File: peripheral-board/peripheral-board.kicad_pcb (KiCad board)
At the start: 2 copper layers, 165 x 130 mm, 264 parts, among them CON4001 BARREL_JACK, CON8001 SD_Card, J10001 DB15_FEMALE_HighDensity, J7001 FCR1295, P10001 VGA, P1001 Peripheral Bus, P1002 Power, Q4001 IRLML2244TRPbF, Q5001 IRLML2244TRPbF, Q5002 IRLML2244TRPbF, Q8001 BSS84LT1G, SW1001 Power, SW2001 1, SW2002 2, SW2003 3, SW2004 4, SW2005 5, SW2006 6, SW2007 7, SW2008 8, SW2009 9, SW2010 0, SW2011 +, SW2012 ´, SW2013 BKSP, SW2014 TROLL, SW2015 §, SW2016 UP, SW2017 RMB, SW2018 Q, SW2019 W, SW2020 E, SW2021 R, SW2022 T, SW2023 Y, SW2024 U, SW2025 I, SW2026 O, SW2027 P, SW2028 Å, SW2029 ¨, SW2030 RETURN, SW2031 ALT_GR, SW2032 <, SW2033 LEFT, SW2034 MMB, SW2035 A, SW2036 S, SW2037 D, SW2038 F, SW2039 G, SW2040 H, SW2041 J, SW2042 K, SW2043 L, SW2044 Ö, SW2045 Ä, SW2046 ', SW2047 ESC, SW2048 TAB, SW2049 ALT, SW2050 DOWN, SW2051 LMB, SW2052 SHIFT_L, SW2053 Z, SW2054 X, SW2055 C, SW2056 V, SW2057 B, SW2058 N, SW2059 M, SW2060 ,, SW2061 ., SW2062 -, SW2063 SHIFT_R, SW2064 FN_R, SW2065 SPACE, SW2066 FN_L, SW2067 RIGHT, SW2068 CTRL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

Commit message: minor fixes
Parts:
- added R2001: 0R, Resistors_SMD:R_1206, F.Cu at (93.9, 73.9)
- moved Q8001 4.01 mm to (91.5, 124.9), turned to 270 degrees
- moved C8002 3.40 mm to (126.2, 116.4)
- moved C8003 2.60 mm to (131.4, 114.2)
- moved D8001 2.55 mm to (173.5, 53.2), turned to 0 degrees
- moved C8004 2.50 mm to (126.2, 114.3)
- moved R4006 1.79 mm to (229.7, 55.6)
- moved R8003 1.50 mm to (178.9, 52.4)
- moved D4002 1.30 mm to (231.1, 53.1)
- moved R4008 1.19 mm to (232.3, 58.0)
- moved R4002 1.14 mm to (232.3, 56.0)
- moved C4001 0.85 mm to (234.8, 52.7)
- moved R4003 0.30 mm to (192.2, 51.3), turned to 180 degrees
- moved D1001 0.20 mm to (159.0, 53.2)
- moved D4003 0.20 mm to (164.9, 53.2)
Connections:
- U2003 pad 10: Net-(U2003-Pad10) -> Net-(R2001-Pad2)
- U2003 pad 6: Net-(U2003-Pad10) -> Net-(R2001-Pad1)
- U2003 pad 9: Net-(U2003-Pad10) -> Net-(R2001-Pad2)
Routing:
- net Net-(D8001-Pad2): track 0.00 -> 176.8 mm, vias 0 -> 2
- net +3V3: track 153.1 -> 246.3 mm, vias 2 -> 10
- net Net-(D4002-Pad1): track 2.51 -> 68.3 mm, vias 0 -> 1
- net GND: track 179.4 -> 232.9 mm, vias 7 -> 14
- net Net-(R4003-Pad1): track 0.00 -> 52.8 mm, vias 0 -> 1
- net Net-(R4004-Pad1): track 0.00 -> 41.2 mm, vias 0 -> 1
- net Net-(D4003-Pad1): track 0.00 -> 27.5 mm
- net Net-(D4003-Pad3): track 0.00 -> 22.5 mm
- net /KBD_Q0: track 430.1 -> 437.0 mm
- net Net-(R2001-Pad2): track 0.00 -> 6.07 mm
- net /KBD_Q1: track 538.7 -> 544.5 mm
- net Net-(D8001-Pad1): track 0.00 -> 5.37 mm
- net Net-(R2001-Pad1): track 0.00 -> 5.17 mm
- net /SPI_SS3: track 43.7 -> 47.7 mm
- net /Keyboard/COL5: track 74.9 -> 78.5 mm
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
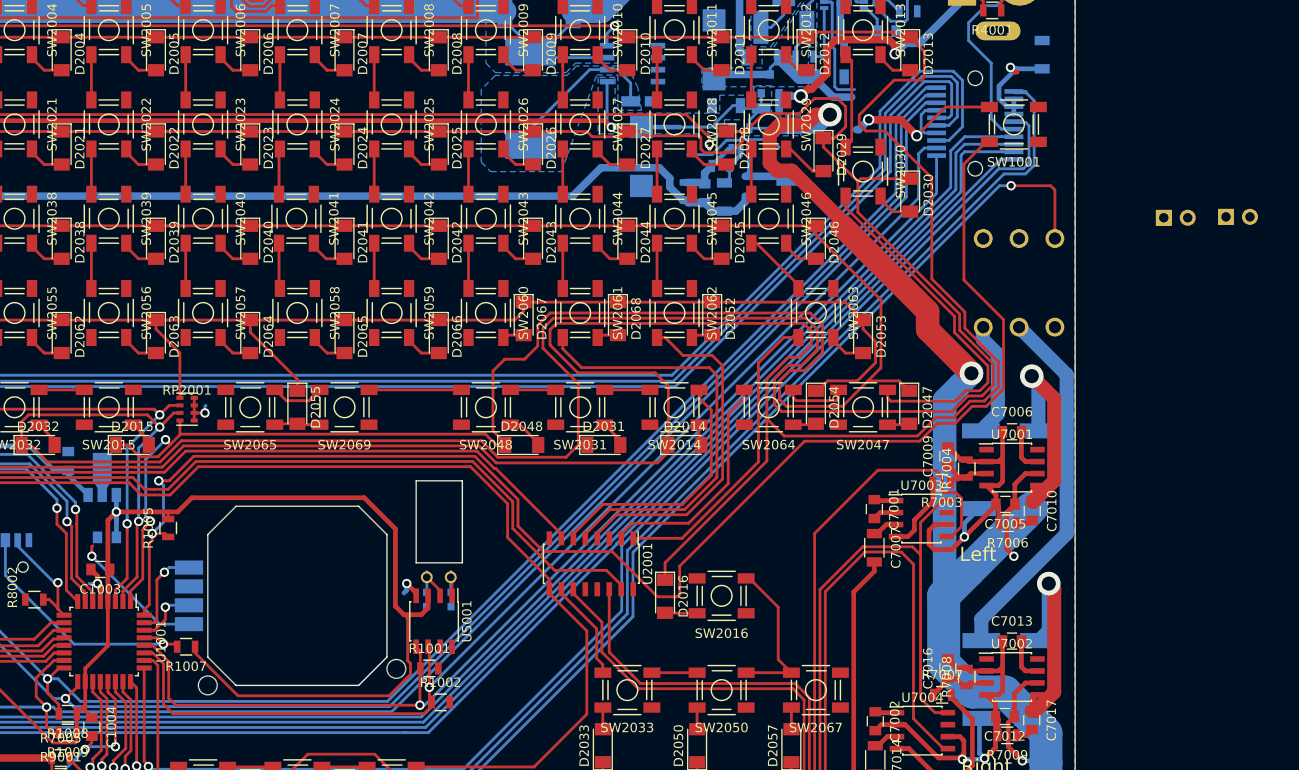
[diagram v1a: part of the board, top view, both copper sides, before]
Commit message: added speaker and battery connectors
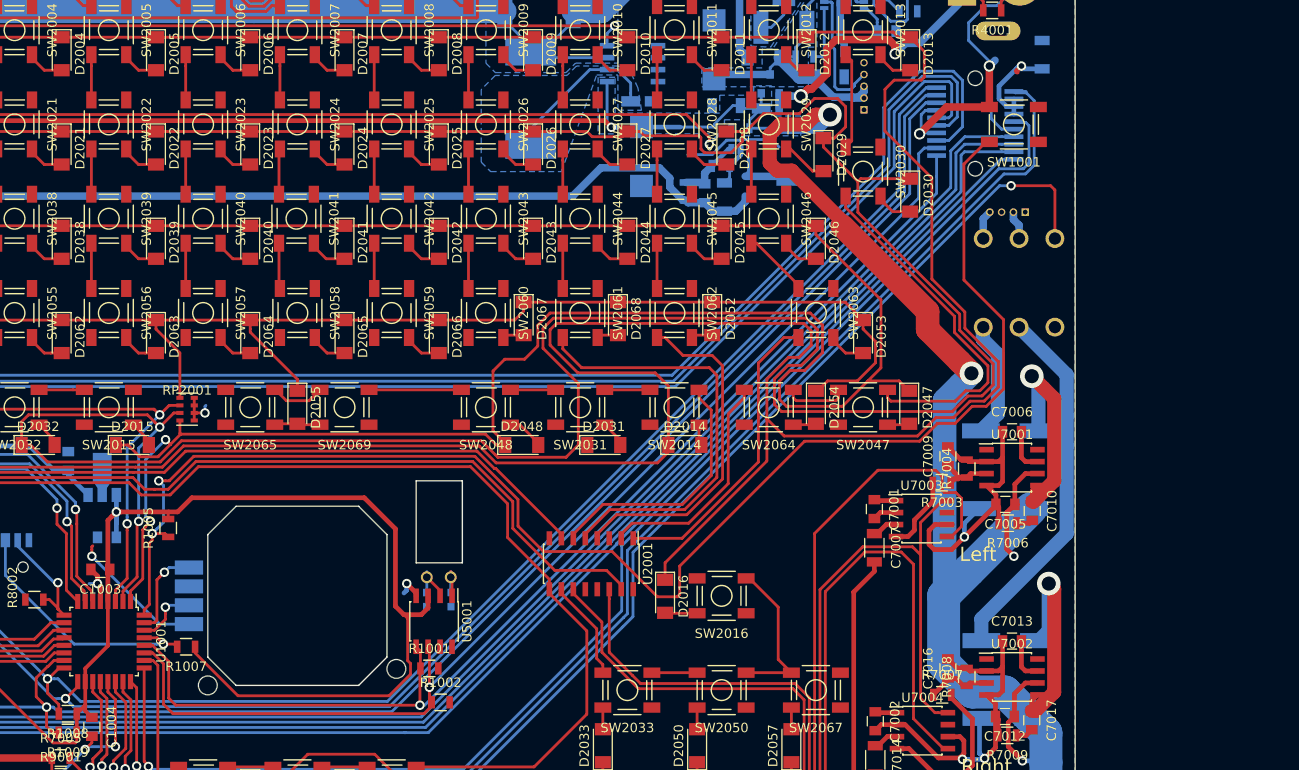
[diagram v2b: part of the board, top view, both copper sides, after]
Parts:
- removed LS7001: Speaker L, Socket_Strips:Socket_Strip_Straight_1x02_Pitch2.54mm
- removed LS7002: Speaker R, Socket_Strips:Socket_Strip_Straight_1x02_Pitch2.54mm
- added J4001: 53047-0510, Connectors_Molex:Connector_Molex_PicoBlade_53047-0510, B.Cu at (227.6, 68.5)
- added J7002: 53047-0310, Connectors_Molex:Connector_Molex_PicoBlade_53047-0410, B.Cu at (244.7, 79.3)
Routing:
- net +BATT: track 30.0 -> 33.5 mm
- net /KBD_Q0: track 437.0 -> 433.5 mm
- net /Audio/SPKR_L: track 0.00 -> 3.09 mm
- net /Audio/SPKR_R: track 0.00 -> 3.05 mm
- net GND: track 232.9 -> 229.9 mm
- net /Power Supply/BATTERY_NTC: track 12.1 -> 13.9 mm

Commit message: peripheral board all done o____O
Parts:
- removed J10001: DB15_FEMALE_HighDensity, lib:HDDSUB-15-VGA
- removed P10001: VGA, Socket_Strips:Socket_Strip_Straight_1x06
- removed Q5001, Q5002: IRLML2244TRPbF, TO_SOT_Packages_SMD:SOT-23
- removed R5001, R5006: 10k, Resistors_SMD:R_0805
- removed R5002, R5007: 150k, Resistors_SMD:R_0805
- removed R5003, R5004, R5008, R5009: 40R, Resistors_SMD:R_0805
- removed R5005, R5010: 220k, Resistors_SMD:R_0805
- removed RV5001, RV5002: 47k, lib:3364W
- removed TH5001: 10k, Capacitors_ThroughHole:CP_Radial_Tantal_D4.5mm_P2.50mm
- removed U5002, U5003: TL431, TO_SOT_Packages_SMD:SOT-23
- moved D2048 1.80 mm to (193.1, 104.0)
- moved R7003 1.10 mm to (234.8, 108.0)
- moved C7007 0.15 mm to (228.7, 115.0)
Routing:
- net GND: track 229.9 -> 291.5 mm, vias 14 -> 19
- net +3V3: track 246.3 -> 261.7 mm
- net /AUD_CS_L: track 145.9 -> 131.0 mm
- net /Keyboard/COL14: track 118.4 -> 123.6 mm
- net /KBD_Q0: track 433.5 -> 438.3 mm
- net /KBD_Q1: track 544.5 -> 548.9 mm
- net /AUD_UD: track 157.4 -> 161.0 mm
- net Net-(C7015-Pad1): track 23.4 -> 26.6 mm
- net Net-(D2048-Pad2): track 3.96 -> 5.64 mm
- net VAA: track 373.0 -> 371.5 mm
- net /KBD_Q2: track 443.8 -> 445.3 mm
- net /PWR_BTN: track 155.8 -> 157.3 mm
- net /Keyboard/COL2: track 177.3 -> 178.8 mm
- net /SD_DET: track 12.2 -> 11.3 mm
- net Net-(C7009-Pad1): track 5.97 -> 6.92 mm
- added copper zone on F.Cu, net GND
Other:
- board size 165 x 130 mm -> 165 x 100 mm

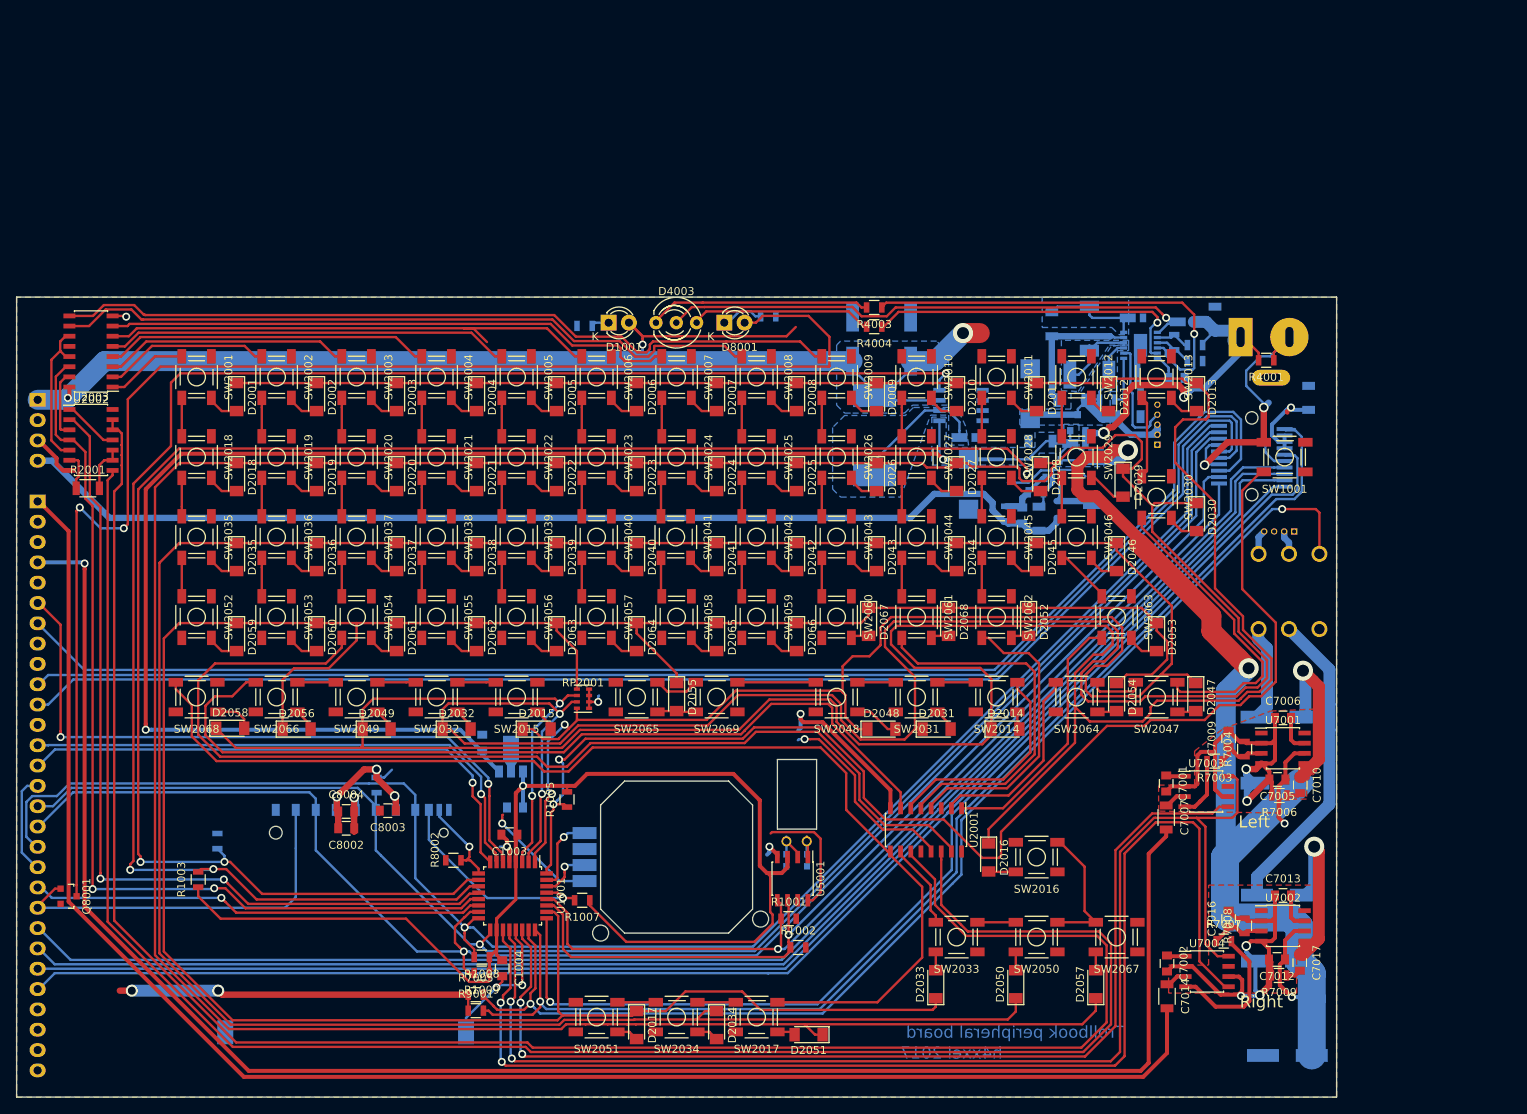
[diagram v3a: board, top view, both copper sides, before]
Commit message: touched up silkscreen
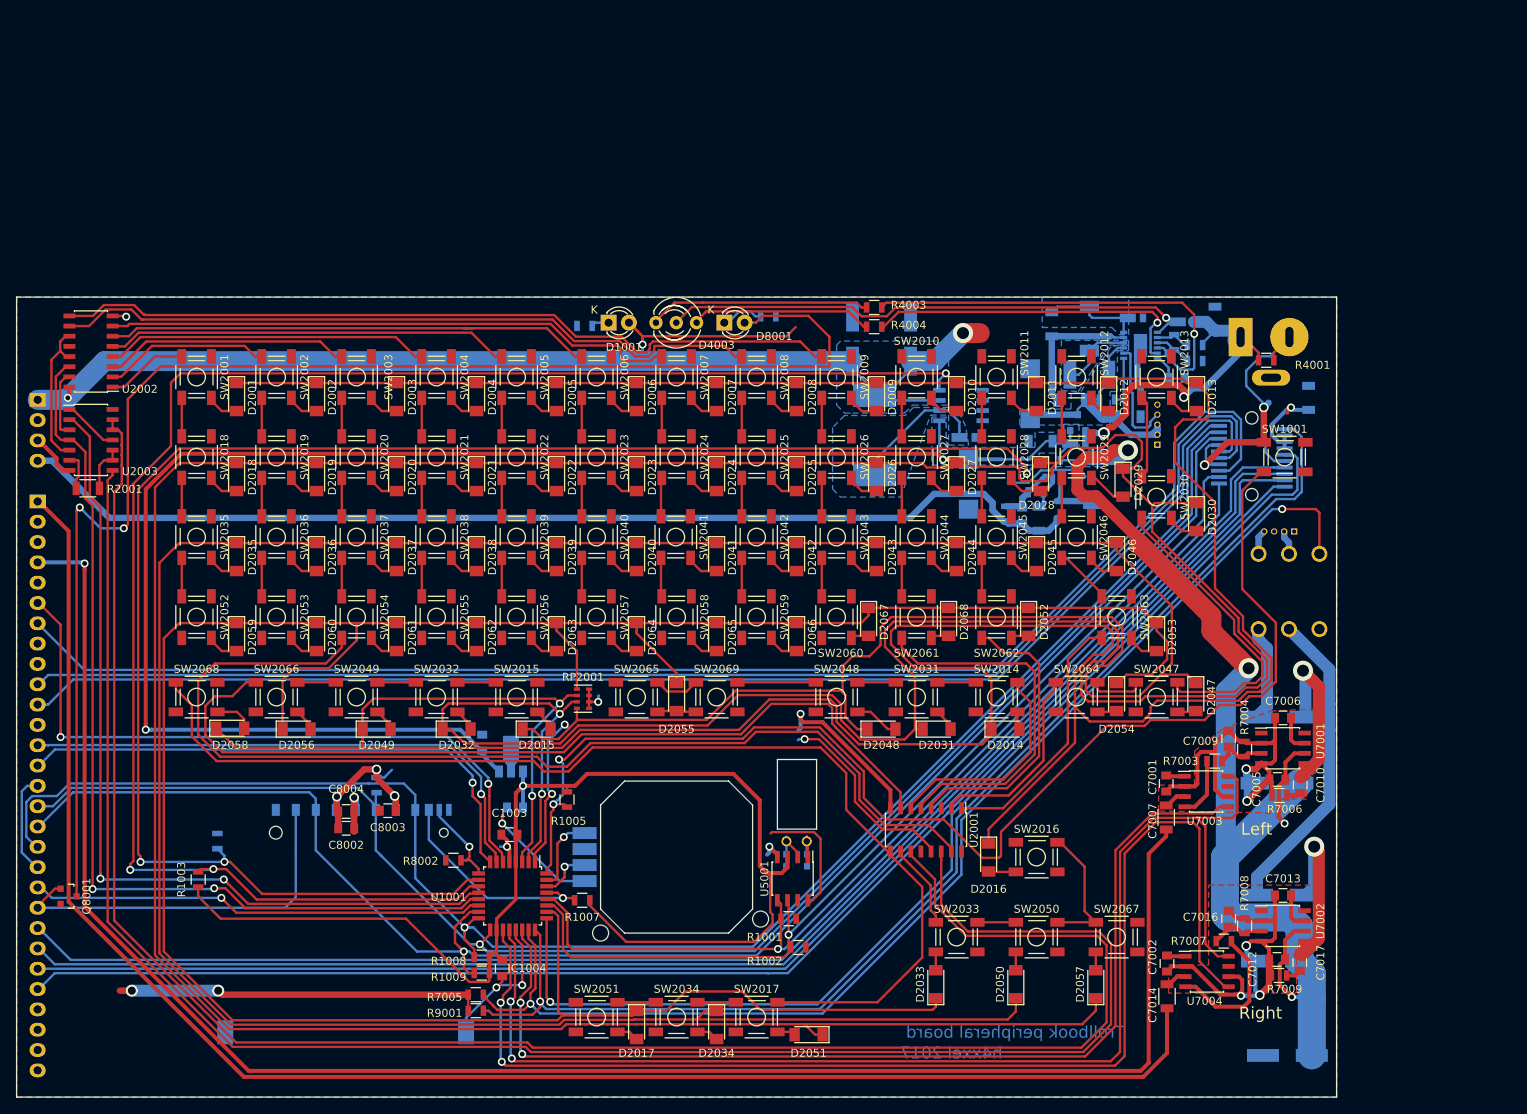
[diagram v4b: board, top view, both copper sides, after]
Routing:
- net /Keyboard/COL5: track 78.5 -> 76.1 mm

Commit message: mouse connected to adc pins
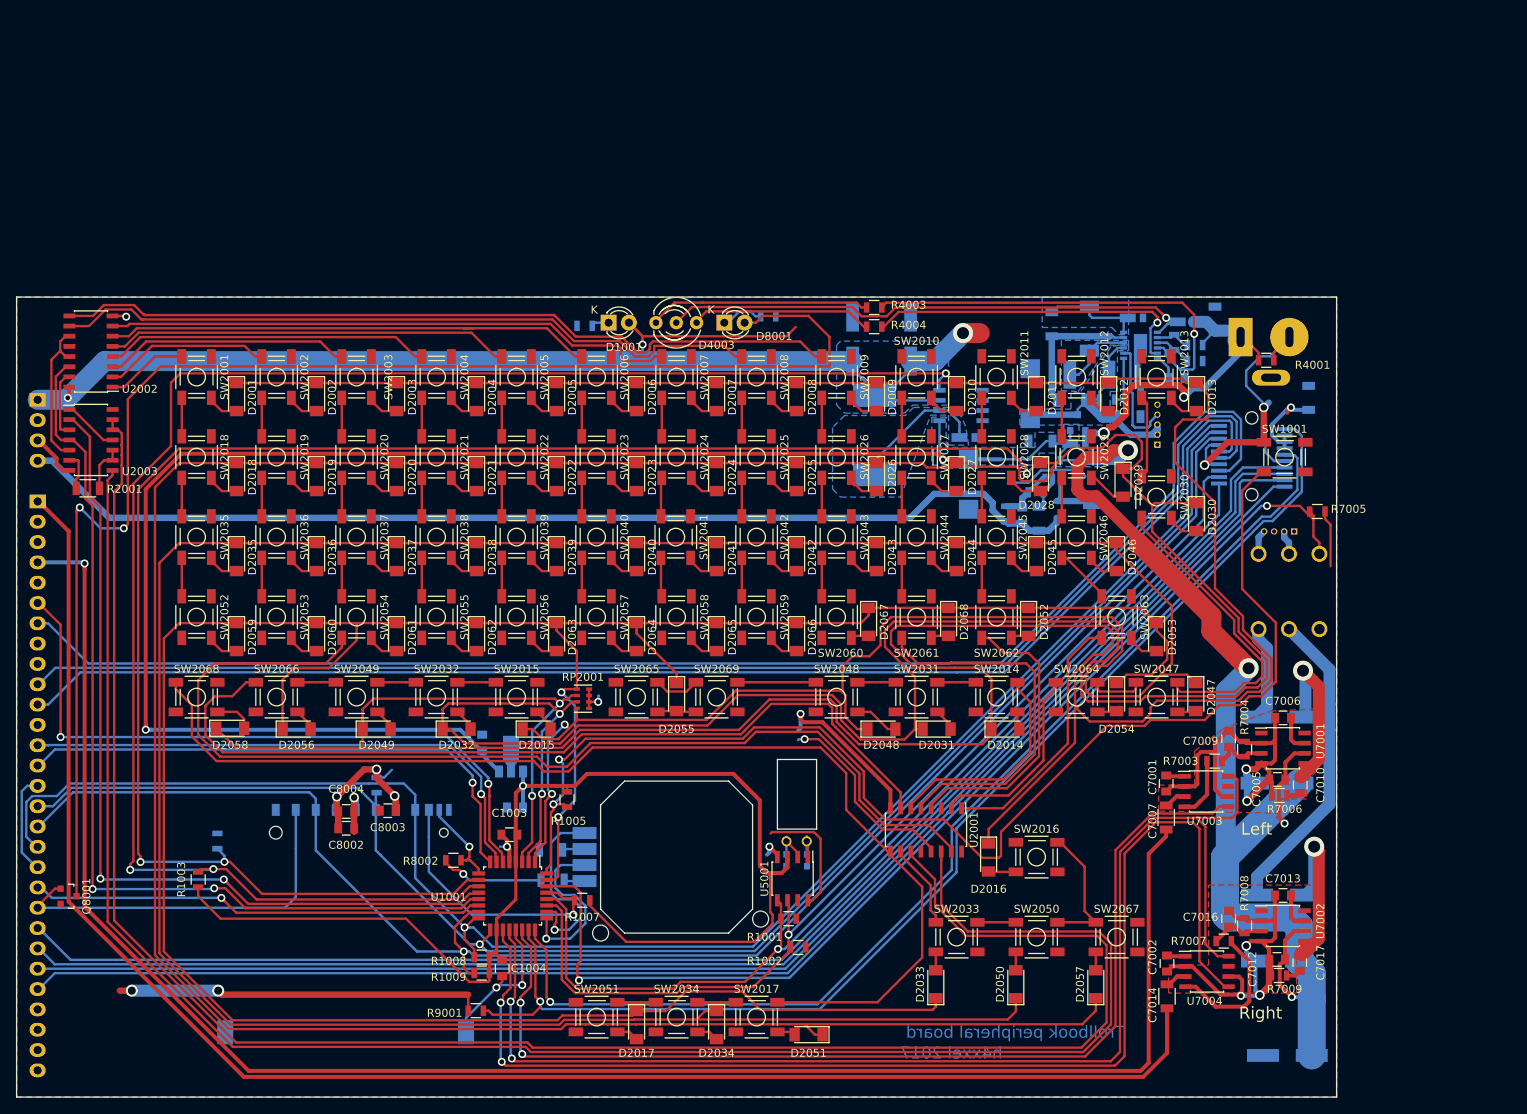
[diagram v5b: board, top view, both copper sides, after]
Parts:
- added R3001: 0, Resistors_SMD:R_1206, B.Cu at (152.0, 122.9)
- added R3002: 0, Resistors_SMD:R_1206, B.Cu at (151.8, 119.1)
- moved R7005 121.3 mm to (247.6, 76.8), turned to 180 degrees
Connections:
- U1001 pad 23: /AUD_DET -> /EXT_DET
- U1001 pad 24: /EXT_DET -> /EXT_AN
- U1001 pad 25: /EXT_AN -> /MOUSE_Y
- U1001 pad 26: /KBD_Q3 -> /MOUSE_X
- U1001 pad 30: /MOUSE_Y -> /AUD_DET
- U1001 pad 31: /MOUSE_X -> /KBD_Q3
- U3001 pad 2: GND -> Net-(R3002-Pad1)
- U3001 pad 4: +3V3 -> Net-(R3001-Pad2)
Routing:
- net /MOUSE_Y: track 6.61 -> 21.3 mm
- net /MOUSE_X: track 9.69 -> 24.2 mm
- net /KBD_Q3: track 335.5 -> 349.5 mm, vias 0 -> 2
- net /AUD_DET: track 151.8 -> 138.8 mm
- net /I2C_SDA: track 123.5 -> 130.4 mm
- net /I2C_SCL: track 121.7 -> 128.6 mm
- net RESET: track 27.4 -> 33.8 mm
- net +3V3: track 261.7 -> 267.7 mm
- net Net-(R3002-Pad1): track 0.00 -> 2.79 mm
- net Net-(R3001-Pad2): track 0.00 -> 2.59 mm
- net /EXT_AN: track 140.6 -> 138.9 mm
- net /EXT_DET: track 155.1 -> 153.8 mm
- net /EXTINT1: track 178.4 -> 177.7 mm
